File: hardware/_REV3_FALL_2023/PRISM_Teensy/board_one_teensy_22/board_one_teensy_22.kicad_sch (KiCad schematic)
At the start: 24 parts, among them J1 Micro_SD_Card_Det_Hirose_DM3AT, J3 3387, U1 Teensy4.0, U3 3966, U4 RFM69HCW_Breakout, U5 SFN-1407PA7.6

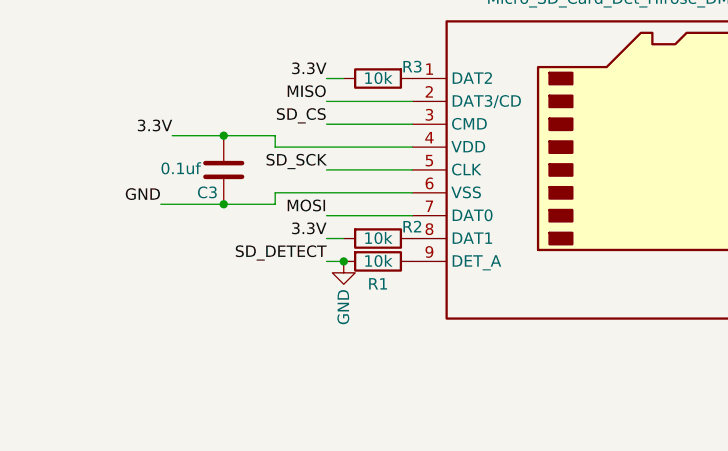
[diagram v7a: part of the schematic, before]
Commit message: Fix SD Detect error
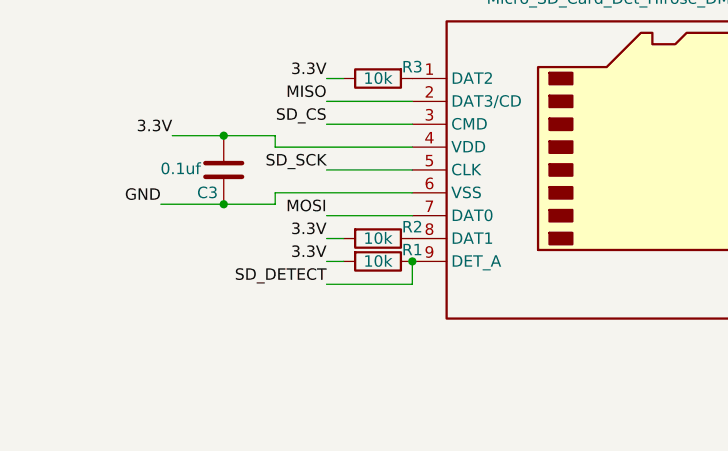
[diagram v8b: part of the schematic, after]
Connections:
- net 3.3V: now also R1.2
- net GND: no longer R1.2, U1.14
- net SD_DETECT: now reaches J1.9 (DET_A), R1.1
- net SD_DETECT: now also U1.14
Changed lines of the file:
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@@
   (junction (at 231.14 27.94) (diameter 0) (color 0 0 0 0)
   )
-  (junction (at 48.26 177.8) (diameter 0) (color 0 0 0 0)
-  )
   (junction (at 34.925 163.83) (diameter 0) (color 0 0 0 0)
   )
@@
   )
   (junction (at 248.92 27.94) (diameter 0) (color 0 0 0 0)
+  )
+  (junction (at 55.88 177.8) (diameter 0) (color 0 0 0 0)
   )
   (junction (at 189.23 99.06) (diameter 0) (color 0 0 0 0)
@@
     (stroke (width 0) (type default))
   )
+  (wire (pts (xy 46.355 177.8) (xy 48.26 177.8))
+    (stroke (width 0) (type default))
+  )
   (wire (pts (xy 129.54 43.18) (xy 138.43 43.18))
     (stroke (width 0) (type default))
@@
     (stroke (width 0) (type default))
   )
-  (wire (pts (xy 46.355 177.8) (xy 48.26 177.8))
-    (stroke (width 0) (type default))
-  )
   (wire (pts (xy 27.94 171.45) (xy 34.925 171.45))
     (stroke (width 0) (type default))
@@
     (stroke (width 0) (type default))
   )
+  (wire (pts (xy 55.88 180.34) (xy 55.88 177.8))
+    (stroke (width 0) (type default))
+  )
+  (wire (pts (xy 46.355 180.34) (xy 55.88 180.34))
+    (stroke (width 0) (type default))
+  )
   (wire (pts (xy 46.355 175.26) (xy 48.26 175.26))
     (stroke (width 0) (type default))
@@
     (effects (font (size 1.27 1.27)) (justify right bottom))
   )
-  (label "SD_DETECT" (at 46.355 177.8 180) (fields_autoplaced)
-    (effects (font (size 1.27 1.27)) (justify right bottom))
-  )
   (label "RX 4" (at 80.01 82.55 0) (fields_autoplaced)
     (effects (font (size 1.27 1.27)) (justify left bottom))
@@
     (effects (font (size 1.27 1.27)) (justify right bottom))
   )
+  (label "SD_DETECT" (at 46.355 180.34 180) (fields_autoplaced)
+    (effects (font (size 1.27 1.27)) (justify right bottom))
+  )
+  (label "3.3V" (at 46.355 177.8 180) (fields_autoplaced)
+    (effects (font (size 1.27 1.27)) (justify right bottom))
+  )
   (label "ARM" (at 182.88 39.37 180) (fields_autoplaced)
     (effects (font (size 1.27 1.27)) (justify right bottom))
@@
   (label "5V" (at 182.88 27.94 180) (fields_autoplaced)
     (effects (font (size 1.27 1.27)) (justify right bottom))
-  )
-  (symbol (lib_name "GND_1") (lib_id "power:GND") (at 48.26 177.8 0) (unit 1)
-    (in_bom yes) (on_board yes) (dnp no)
-    (property "Reference" "#PWR04" (at 48.26 184.15 0)
-      (effects (font (size 1.27 1.27)) hide)
-    )
-    (property "Value" "GND" (at 48.26 182.88 90)
-      (effects (font (size 1.27 1.27)))
-    )
-    (property "Footprint" "" (at 48.26 177.8 0)
-      (effects (font (size 1.27 1.27)) hide)
-    )
-    (property "Datasheet" "" (at 48.26 177.8 0)
-      (effects (font (size 1.27 1.27)) hide)
-    )
-    (pin "1")
-    (instances
-      (project "board_one_teensy_22"
-        (path "/7a48c3b0-2761-409e-ae2f-7ebae3820225"
-          (reference "#PWR04") (unit 1)
-        )
-      )
-    )
   )
   (symbol (lib_id "Connector:Conn_01x04_Socket") (at 187.96 27.94 0) (unit 1)
@@
   (symbol (lib_id "Device:R") (at 52.07 177.8 270) (unit 1)
     (in_bom yes) (on_board yes) (dnp no)
-    (property "Reference" "R1" (at 52.07 180.34 90)
-      (effects (font (size 1.27 1.27)))
-    )
+    (property "Reference" "R1" (at 55.88 176.53 90)
+      (effects (font (size 1.27 1.27)))
+    )
